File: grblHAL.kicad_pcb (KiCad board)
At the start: 4 copper layers, 150 x 105 mm, 279 parts, among them J1 Screw_Terminal_01x08, J10 Screw_Terminal_01x08, J11 Screw_Terminal_01x04x3, J12 Screw_Terminal_01x02, J13 Conn_ARM_JTAG_SWD_10, J14 Conn_01x03_Pin, J15 Conn_01x03_Pin, J16 Conn_01x02_Pin, J17 Conn_01x02_Pin, J18 Conn_01x03_Pin, J19 Screw_Terminal_01x02x5, J2 Screw_Terminal_01x08, J20 Conn_01x02_Pin, J21 Screw_Terminal_01x02, J22 Screw_Terminal_01x04x3, J23 Conn_01x03_Pin, J24 Conn_01x03_Pin, J25 Conn_01x03_Pin, J26 Conn_01x03_Pin, J27 Conn_01x03_Pin, J28 Conn_01x03_Pin, J29 Conn_01x03_Pin, J3 Screw_Terminal_01x08, J30 Conn_01x03_Pin, J31 Conn_01x03_Pin, J32 Conn_01x03_Pin, J33 Conn_01x03_Pin, J34 Conn_01x03_Pin, J35 Conn_01x03_Pin, J36 Conn_01x03_Pin, J37 Conn_01x03_Pin, J38 Conn_01x03_Pin, J39 Conn_01x03_Pin, J4 Screw_Terminal_01x06, J40 Conn_01x03_Pin, J41 Conn_01x03_Pin, J42 Conn_01x03_Pin, J43 USB_B, J44 Conn_01x08_Pin, J5 Screw_Terminal_01x06, J6 Screw_Terminal_01x02, J7 Screw_Terminal_01x08, J8 Screw_Terminal_01x02, J9 Screw_Terminal_01x08, SW1 SW_Push, SW2 SW_Push, U1 STM32F407VETx, U10 74HC2G34, U11 74HC2G34, U12 74HC2G34, U13 74HC2G34, U14 74HC2G34, U15 MCP6004, U16 ULN2803A, U17 ELQ3H4(TA)-G, U18 ELQ3H4(TA)-G, U19 ELQ3H4(TA)-G, U2 MAX3078E, U20 ELQ3H4(TA)-G, U21 74HC2G34, U22 74HC2G34, U23 74HC2G34, U24 USBLC6-2P6, U25 LM358, U26 SN74LVC245APW, U3 AMS1117-3.3, U4 LMR51430, U5 LMR51430, U6 MCP6004, U7 ELQ3H4(TA)-G, U8 74HC2G34, U9 74HC2G34, Y1 8Mhz

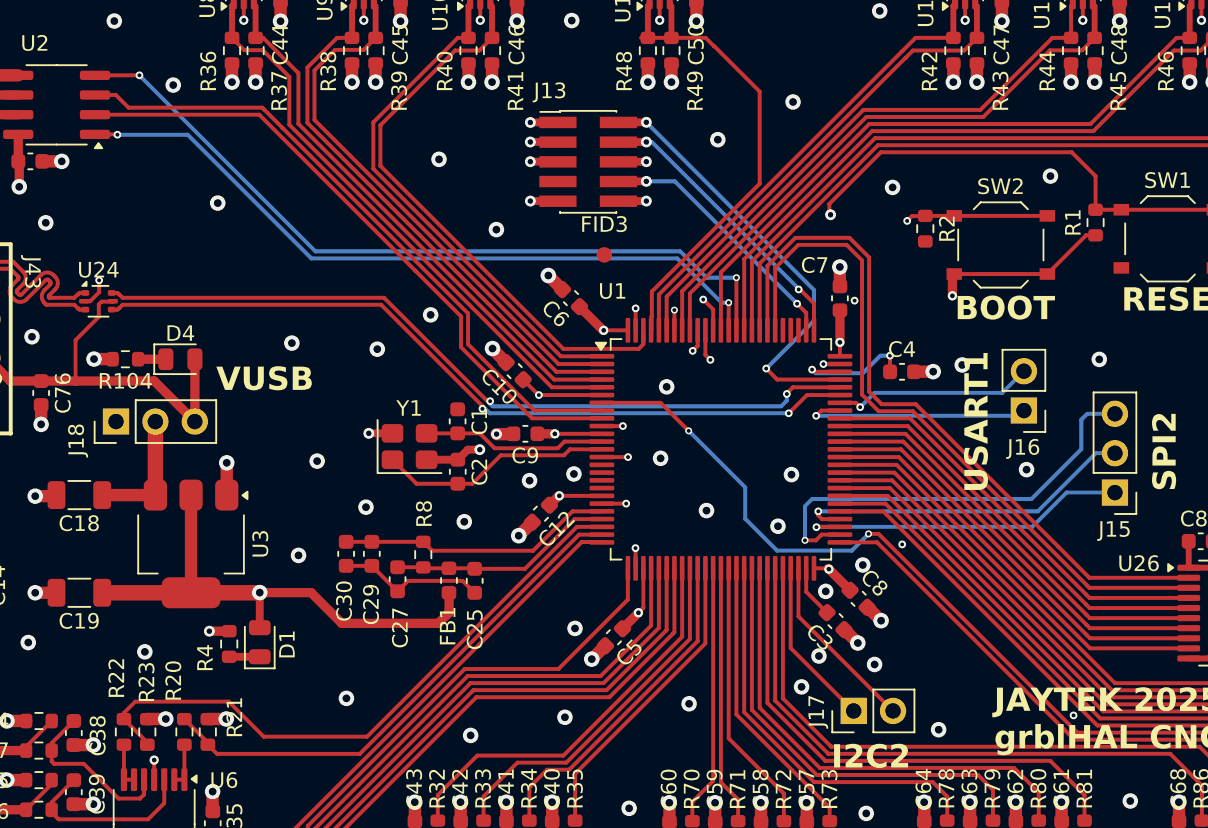
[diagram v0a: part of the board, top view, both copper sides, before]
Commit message: moved rs485 re/de lines, start of manual
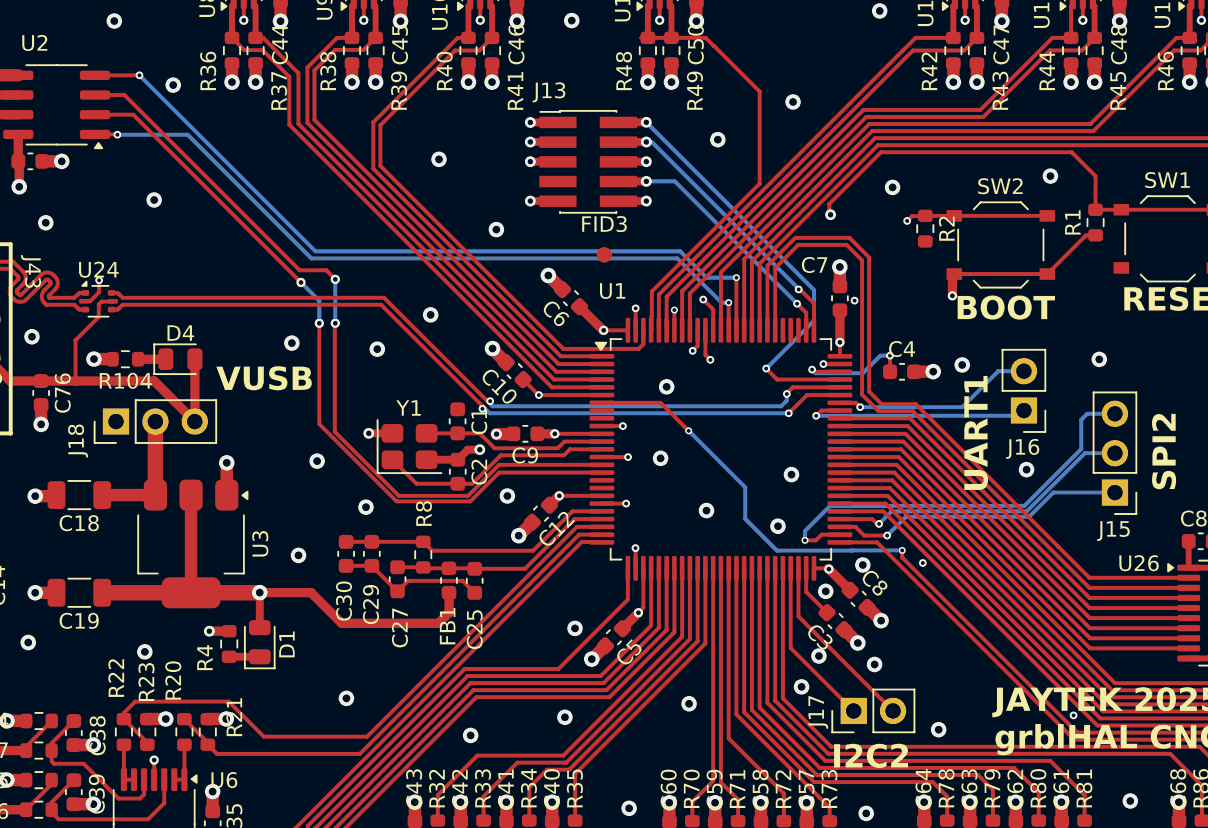
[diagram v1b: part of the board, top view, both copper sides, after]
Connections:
- net /PWM renamed /buffer driver10/INPUT_B
- U1 pad 15: unconnected-(U1-PC0-Pad15) -> /MCU/DRIVER_ENABLE
- U1 pad 16: unconnected-(U1-PC1-Pad16) -> /MCU/RECEIVER_ENABLE
- U1 pad 8: /MCU/DRIVER_ENABLE -> unconnected-(U1-PC14-Pad8)
- U1 pad 9: /MCU/RECEIVER_ENABLE -> unconnected-(U1-PC15-Pad9)
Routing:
- net /MCU/DRIVER_ENABLE: track 42.3 -> 50.1 mm, vias 0 -> 2
- net /MCU/RECEIVER_ENABLE: track 42.0 -> 48.4 mm, vias 0 -> 2
- net +3V3: track 226.4 -> 223.4 mm
- net /MCU/SPI2_MOSI: track 22.3 -> 19.7 mm
- net /MCU/SPI2_MISO: track 21.6 -> 19.0 mm
- net /MCU/SPI2_SCK: track 28.2 -> 27.3 mm
- net /MCU/AUX_INPUT_3: track 61.7 -> 61.0 mm
- net GND: vias 305 -> 303
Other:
- board text added: "UART1"
- board text removed: "USART1"
